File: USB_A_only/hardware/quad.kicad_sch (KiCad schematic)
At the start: 37 parts, among them J1 USB_C_Receptacle_USB2.0, J2 USB_A, J3 USB_A, J4 USB_A, J5 USB_A, U1 FE1.1s, Y1 Crystal

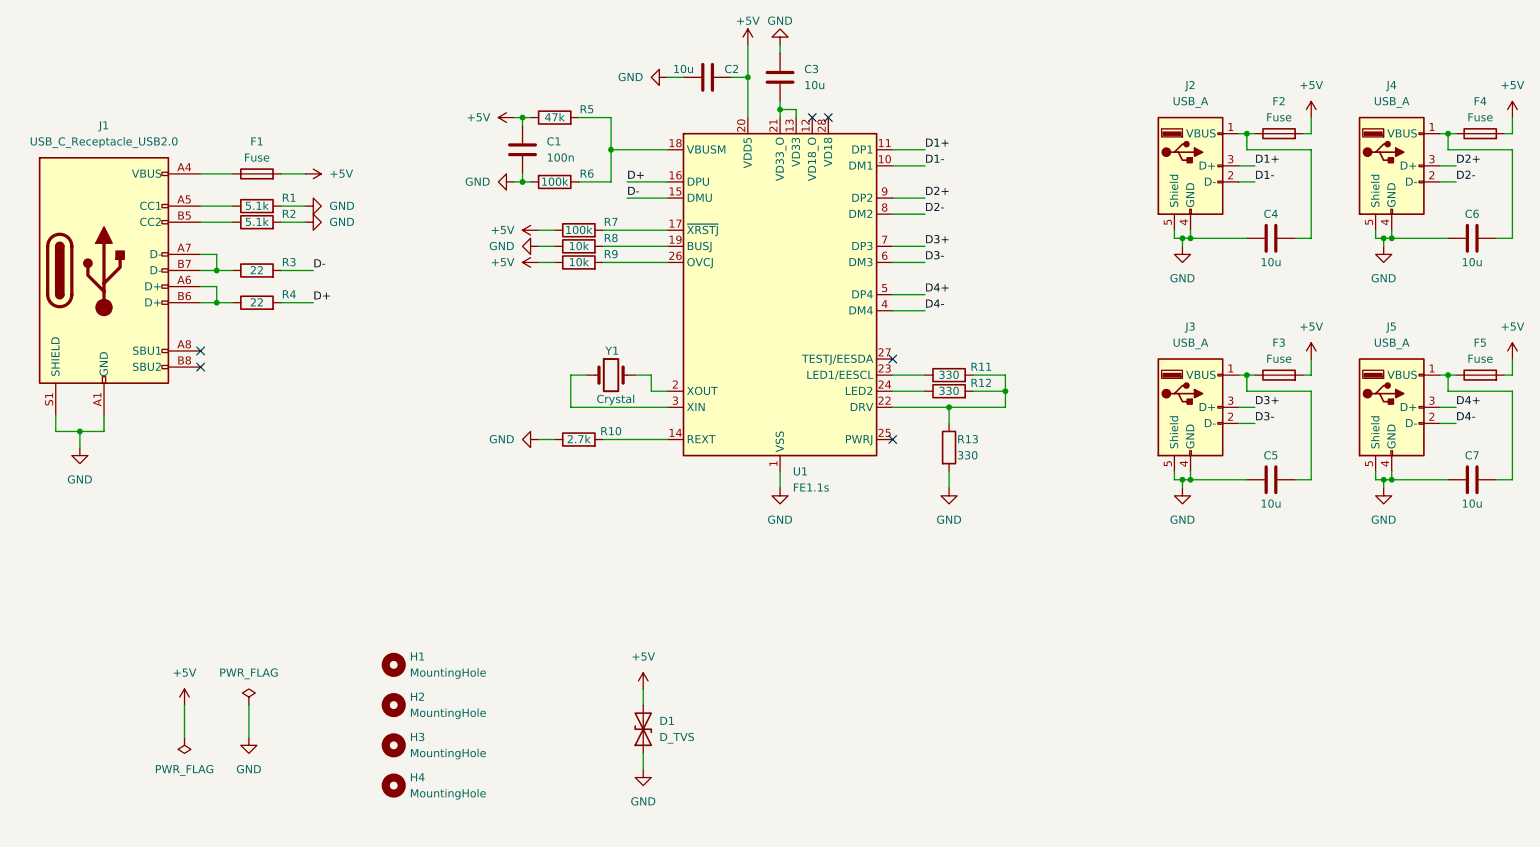
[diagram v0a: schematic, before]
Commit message: Change the IC from FE1.1s to SL2.2s, and release the schematic v1.0_alpha
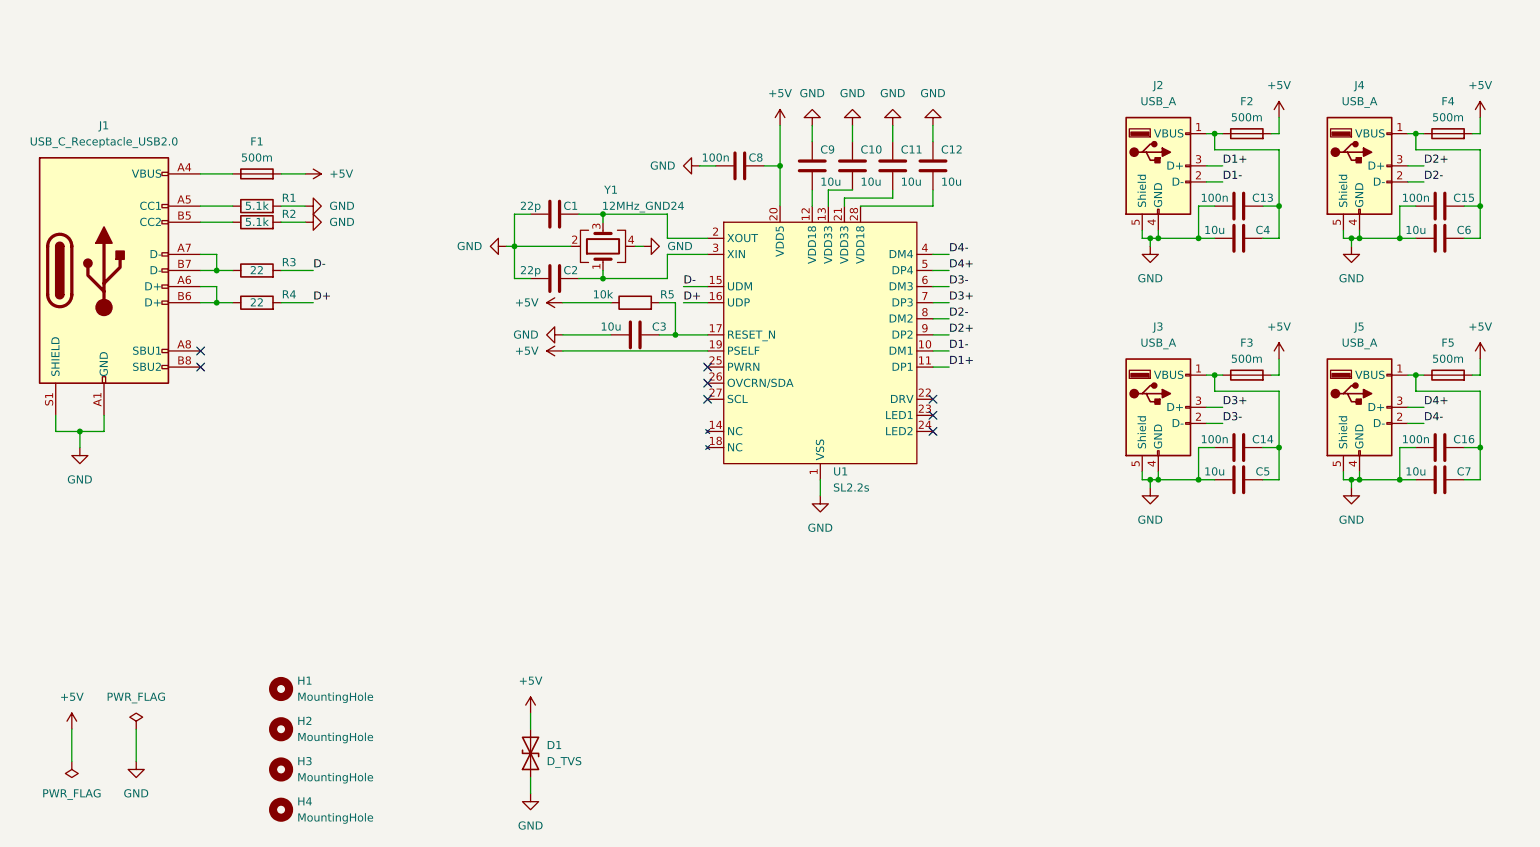
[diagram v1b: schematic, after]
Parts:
- removed R10: 2.7k, Resistor_SMD:R_0603_1608Metric_Pad0.98x0.95mm_HandSolder, symbol Device:R
- removed R11, R12, R13: 330, Resistor_SMD:R_0603_1608Metric_Pad0.98x0.95mm_HandSolder, symbol Device:R
- removed R6, R7: 100k, Resistor_SMD:R_0603_1608Metric_Pad0.98x0.95mm_HandSolder, symbol Device:R
- removed R8, R9: 10k, Resistor_SMD:R_0603_1608Metric_Pad0.98x0.95mm_HandSolder, symbol Device:R
- removed U1: FE1.1s, Package_SO:SSOP-28_3.9x9.9mm_P0.635mm, symbol Interface_USB:FE1.1s
- removed Y1: Crystal, Crystal:Crystal_SMD_HC49-SD, symbol Device:Crystal
- added C10, C11, C12, C9: 10u, Capacitor_SMD:C_0603_1608Metric, symbol Device:C
- added C13, C14, C15, C16, C8: 100n, Capacitor_SMD:C_0603_1608Metric, symbol Device:C
- added U1: SL2.2s, Package_SO:SSOP-28_3.9x9.9mm_P0.635mm, symbol Lib:SL2.2s
- added Y1: 12MHz_GND24, Crystal:Crystal_SMD_3225-4Pin_3.2x2.5mm, symbol Device:Crystal_GND24
- C1: value 100n -> 22p; footprint Capacitor_SMD:C_0603_1608Metric_Pad1.08x0.95mm_HandSolder -> Capacitor_SMD:C_0603_1608Metric
- C2: value 10u -> 22p; footprint Capacitor_SMD:C_0603_1608Metric_Pad1.08x0.95mm_HandSolder -> Capacitor_SMD:C_0603_1608Metric
- C3, C4, C5, C6, C7: footprint Capacitor_SMD:C_0603_1608Metric_Pad1.08x0.95mm_HandSolder -> Capacitor_SMD:C_0603_1608Metric
- F1, F2, F3, F4, F5: value Fuse -> 500m; footprint Fuse:Fuse_0603_1608Metric_Pad1.05x0.95mm_HandSolder -> Fuse:Fuse_0603_1608Metric
- R1, R2, R3, R4: footprint Resistor_SMD:R_0603_1608Metric_Pad0.98x0.95mm_HandSolder -> Resistor_SMD:R_0603_1608Metric
- R5: value 47k -> 10k; footprint Resistor_SMD:R_0603_1608Metric_Pad0.98x0.95mm_HandSolder -> Resistor_SMD:R_0603_1608Metric
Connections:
- net +5V: now also C8.2, U1.19 (PSELF), U1.20 (VDD5); no longer C1.1, C2.2
- net D+: now also U1.16 (UDP)
- net D-: now also U1.15 (UDM)
- net D1+: now also U1.11 (DP1)
- net D1-: now also U1.10 (DM1)
- net D2+: now also U1.9 (DP2)
- net D2-: now also U1.8 (DM2)
- net D3+: now also U1.7 (DP3)
- net D3-: now also U1.6 (DM3)
- net D4+: now also U1.5 (DP4)
- net D4-: now also U1.4 (DM4)
- net GND: now also C1.1, C10.1, C11.1, C12.1, C13.1, C14.1, C15.1, C16.1, C8.1, C9.1, U1.1 (VSS), Y1.2, Y1.4; no longer C1.2
- net at C7.2, F5.1, J5.1 (VBUS): now also C16.2
- net at R5.2: now also C3.2, U1.17 (RESET_N)
- net at C5.2, F3.1, J3.1 (VBUS): now also C14.2
- net at C6.2, F4.1, J4.1 (VBUS): now also C15.2
- net at C4.2, F2.1, J2.1 (VBUS): now also C13.2
- new net: C11.2, U1.21 (VDD33)
- new net: C2.2, U1.3 (XIN), Y1.1
- new net: C1.2, U1.2 (XOUT), Y1.3
- new net: C9.2, U1.12 (VDD18)
- new net: C10.2, U1.13 (VDD33)
- new net: C12.2, U1.28 (VDD18)
- no-connect marks 6 -> 8
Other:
- title: (none) -> quad
- moved on the sheet: C4, C5, C6, C7, D1, F2, F3, F4, F5, H1, H2, H3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

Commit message: Release the PCB v1.0_alpha
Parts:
- added C17: 10u, Capacitor_SMD:C_0603_1608Metric, symbol Device:C
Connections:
- net GND: now also C17.1
- net at F1.1, J1.A4 (VBUS), J1.A9 (VBUS)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: now also C17.2
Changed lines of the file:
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@@
   (junction (at 251.46 78.74) (diameter 0) (color 0 0 0 0)
+  )
+  (junction (at 64.77 68.58) (diameter 0) (color 0 0 0 0)
   )
   (junction (at 243.84 116.84) (diameter 0) (color 0 0 0 0)
@@
     (stroke (width 0) (type default) (color 0 0 0 0))
   )
-  (wire (pts (xy 62.23 68.58) (xy 67.31 68.58))
+  (wire (pts (xy 62.23 68.58) (xy 64.77 68.58))
     (stroke (width 0) (type default) (color 0 0 0 0))
   )
@@
     (stroke (width 0) (type default) (color 0 0 0 0))
   )
+  (wire (pts (xy 64.77 60.96) (xy 64.77 68.58))
+    (stroke (width 0) (type default) (color 0 0 0 0))
+  )
   (wire (pts (xy 229.87 111.76) (xy 232.41 111.76))
     (stroke (width 0) (type default) (color 0 0 0 0))
@@
     (stroke (width 0) (type default) (color 0 0 0 0))
   )
+  (wire (pts (xy 64.77 50.8) (xy 64.77 53.34))
+    (stroke (width 0) (type default) (color 0 0 0 0))
+  )
   (wire (pts (xy 111.76 74.93) (xy 111.76 80.01))
     (stroke (width 0) (type default) (color 0 0 0 0))
@@
   )
   (wire (pts (xy 245.11 78.74) (xy 243.84 78.74))
+    (stroke (width 0) (type default) (color 0 0 0 0))
+  )
+  (wire (pts (xy 64.77 68.58) (xy 67.31 68.58))
     (stroke (width 0) (type default) (color 0 0 0 0))
   )
@@
     (pin "1")
     (pin "2")
+  )
+  (symbol (lib_id "power:GND") (at 64.77 50.8 180) (unit 1)
+    (in_bom yes) (on_board yes) (fields_autoplaced)
+    (property "Reference" "#PWR029" (id 0) (at 64.77 44.45 0)
+      (effects (font (size 1.27 1.27)) hide)
+    )
+    (property "Value" "GND" (id 1) (at 64.77 45.72 0))
+    (property "Footprint" "" (id 2) (at 64.77 50.8 0)
+      (effects (font (size 1.27 1.27)) hide)
+    )
+    (property "Datasheet" "" (id 3) (at 64.77 50.8 0)
+      (effects (font (size 1.27 1.27)) hide)
+    )
+    (pin "1")
   )
   (symbol (lib_id "Connector:USB_C_Receptacle_USB2.0") (at 46.99 83.82 0) (unit 1)
@@
     (pin "1")
   )
+  (symbol (lib_id "Device:C") (at 64.77 57.15 0) (unit 1)
+    (in_bom yes) (on_board yes)
+    (property "Reference" "C17" (id 0) (at 66.04 54.61 0)
+      (effects (font (size 1.27 1.27)) (justify left))
+    )
+    (property "Value" "10u" (id 1) (at 66.04 59.69 0)
+      (effects (font (size 1.27 1.27)) (justify left))
+    )
+    (property "Footprint" "Capacitor_SMD:C_0603_1608Metric" (id 2) (at 65.7352 60.96 0)
+      (effects (font (size 1.27 1.27)) hide)
+    )
+    (property "Datasheet" "~" (id 3) (at 64.77 57.15 0)
+      (effects (font (size 1.27 1.27)) hide)
+    )
+    (pin "1")
+    (pin "2")
+  )
   (symbol (lib_id "power:+5V") (at 78.74 68.58 270) (unit 1)
     (in_bom yes) (on_board yes) (fields_autoplaced)
@@
       (reference "#PWR028") (unit 1) (value "GND") (footprint "")
     )
+    (path "/efcc270a-dc30-4a57-976a-ee88f06afc16"
+      (reference "#PWR029") (unit 1) (value "GND") (footprint "")
+    )
     (path "/4455bacd-ab30-43b7-8ce8-17fe1f34c3d9"
       (reference "C1") (unit 1) (value "22p") (footprint "Capacitor_SMD:C_0603_1608Metric")
@@
       (reference "C16") (unit 1) (value "100n") (footprint "Capacitor_SMD:C_0603_1608Metric")
     )
+    (path "/f65c43e5-24a0-461e-8408-700365ad8bfc"
+      (reference "C17") (unit 1) (value "10u") (footprint "Capacitor_SMD:C_0603_1608Metric")
+    )
     (path "/d859cae6-9ef8-4a46-81ad-89d6ac99fc1a"
